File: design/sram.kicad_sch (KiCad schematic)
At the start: 43 parts, among them U10 IS61WV12816EDBLL-10TLI

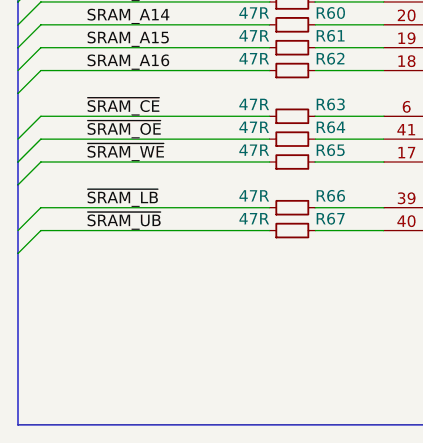
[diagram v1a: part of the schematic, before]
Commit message: Refactored FPGA schematic
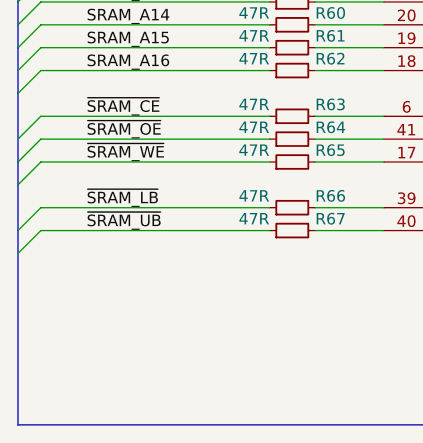
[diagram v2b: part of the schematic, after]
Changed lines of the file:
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@@
-(kicad_sch (version 20200512) (host eeschema "5.99.0-unknown-ad88874~101~ubuntu18.04.1")
-  (page 6 8)
+(kicad_sch (version 20200512) (host eeschema "5.99.0-unknown-92ce7ca~101~ubuntu18.04.1")
+  (page 1 8)
   (paper "A4")
   (title_block
@@
   (bus (pts (xy 36.83 101.6) (xy 36.83 106.68)))
   (bus (pts (xy 36.83 106.68) (xy 36.83 114.3)))
-  (bus (pts (xy 36.83 114.3) (xy 36.83 116.84)))
-  (bus (pts (xy 36.83 116.84) (xy 36.83 124.46)))
-  (bus (pts (xy 36.83 124.46) (xy 36.83 143.51)))
+  (bus (pts (xy 36.83 114.3) (xy 36.83 121.92)))
+  (bus (pts (xy 36.83 121.92) (xy 36.83 143.51)))
   (bus (pts (xy 36.83 143.51) (xy 158.75 143.51)))
   (bus (pts (xy 158.75 63.5) (xy 158.75 68.58)))

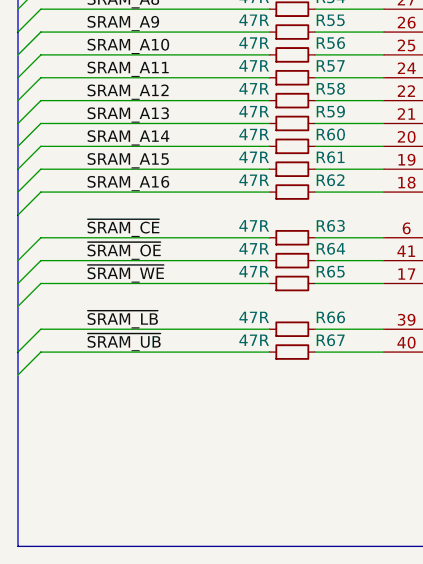
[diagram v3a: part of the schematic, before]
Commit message: Added oscilator layout
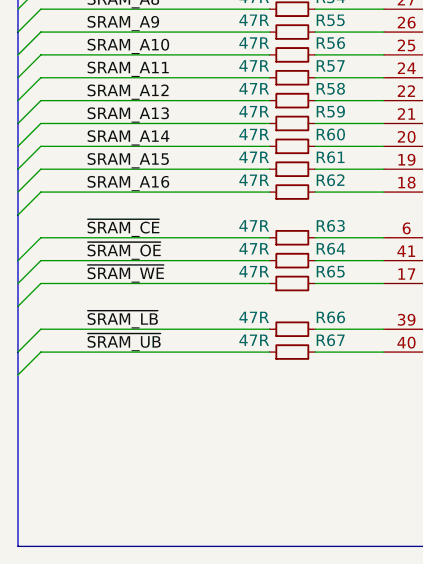
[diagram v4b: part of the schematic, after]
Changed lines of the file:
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@@
-(kicad_sch (version 20200512) (host eeschema "5.99.0-unknown-92ce7ca~101~ubuntu18.04.1")
+(kicad_sch (version 20200512) (host eeschema "5.99.0-unknown-0658d29~101~ubuntu18.04.1")
   (page 6 8)
   (paper "A4")
@@
   (bus (pts (xy 36.83 96.52) (xy 36.83 101.6)))
   (bus (pts (xy 36.83 101.6) (xy 36.83 106.68)))
-  (bus (pts (xy 36.83 106.68) (xy 36.83 114.3)))
-  (bus (pts (xy 36.83 114.3) (xy 36.83 121.92)))
+  (bus (pts (xy 36.83 106.68) (xy 36.83 111.76)))
+  (bus (pts (xy 36.83 111.76) (xy 36.83 116.84)))
+  (bus (pts (xy 36.83 116.84) (xy 36.83 121.92)))
   (bus (pts (xy 36.83 121.92) (xy 36.83 143.51)))
   (bus (pts (xy 36.83 143.51) (xy 158.75 143.51)))

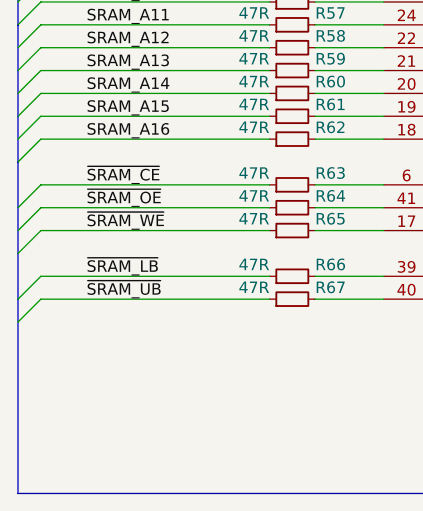
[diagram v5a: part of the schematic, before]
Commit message: Fixed MCU RST
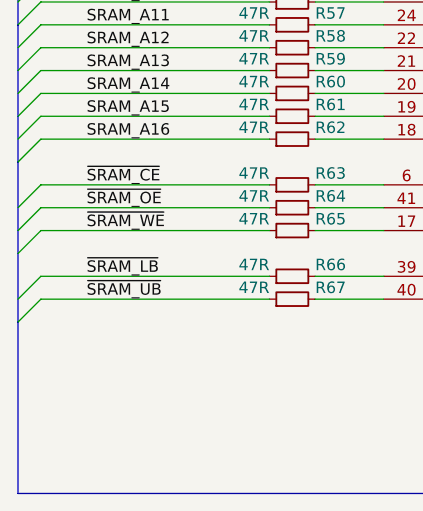
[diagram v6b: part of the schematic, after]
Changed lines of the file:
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@@
   (bus (pts (xy 36.83 96.52) (xy 36.83 101.6)))
   (bus (pts (xy 36.83 101.6) (xy 36.83 106.68)))
-  (bus (pts (xy 36.83 106.68) (xy 36.83 111.76)))
-  (bus (pts (xy 36.83 111.76) (xy 36.83 116.84)))
-  (bus (pts (xy 36.83 116.84) (xy 36.83 121.92)))
-  (bus (pts (xy 36.83 121.92) (xy 36.83 143.51)))
+  (bus (pts (xy 36.83 106.68) (xy 36.83 114.3)))
+  (bus (pts (xy 36.83 114.3) (xy 36.83 116.84)))
+  (bus (pts (xy 36.83 116.84) (xy 36.83 124.46)))
+  (bus (pts (xy 36.83 124.46) (xy 36.83 143.51)))
   (bus (pts (xy 36.83 143.51) (xy 158.75 143.51)))
   (bus (pts (xy 158.75 63.5) (xy 158.75 68.58)))

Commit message: Updated some layout
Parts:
- renumbered C53 to C57, C54 to C58, C55 to C59, C56 to C60, R46 to R49, R47 to R50, R48 to R51, R49 to R52, R50 to R53, R51 to R54, R52 to R55, R53 to R56, R54 to R57, R55 to R58, R56 to R59, R57 to R60, R58 to R61, R59 to R62, R60 to R63, R61 to R64, R62 to R65, R63 to R66, R64 to R67, R65 to R68, R66 to R69, R67 to R70, R68 to R71, R69 to R72, R70 to R73, R71 to R74, R72 to R75, R73 to R76, R74 to R77, R75 to R78, R76 to R79, R77 to R80, R78 to R81, R79 to R82, R80 to R83, R81 to R84, R82 to R85, R83 to R86, U10 to U11

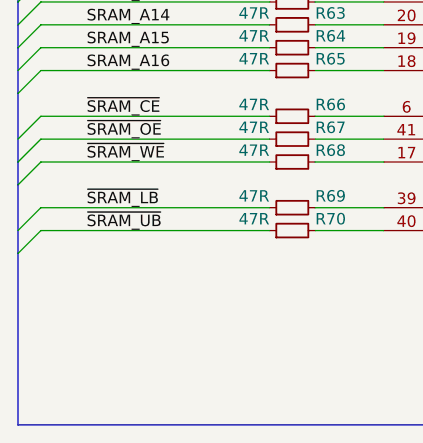
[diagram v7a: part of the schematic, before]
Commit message: Added logo and description to F.Silks
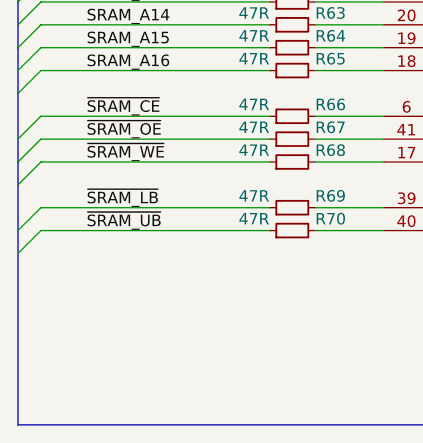
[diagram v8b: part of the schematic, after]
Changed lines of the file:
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@@
-(kicad_sch (version 20200512) (host eeschema "5.99.0-unknown-d72a778~101~ubuntu18.04.1")
+(kicad_sch (version 20200512) (host eeschema "5.99.0-unknown-4efed4b~101~ubuntu18.04.1")
   (page 6 8)
   (paper "A4")
@@
   (bus (pts (xy 36.83 101.6) (xy 36.83 106.68)))
   (bus (pts (xy 36.83 106.68) (xy 36.83 114.3)))
-  (bus (pts (xy 36.83 114.3) (xy 36.83 116.84)))
-  (bus (pts (xy 36.83 116.84) (xy 36.83 124.46)))
-  (bus (pts (xy 36.83 124.46) (xy 36.83 143.51)))
+  (bus (pts (xy 36.83 114.3) (xy 36.83 121.92)))
+  (bus (pts (xy 36.83 121.92) (xy 36.83 143.51)))
   (bus (pts (xy 36.83 143.51) (xy 158.75 143.51)))
   (bus (pts (xy 158.75 63.5) (xy 158.75 68.58)))
